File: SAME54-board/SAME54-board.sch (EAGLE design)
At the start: 33 parts, among them IC1 ATSAME54N20A-AUT, J1 GSD09002SEU, J2 CON-SOCJ-2155

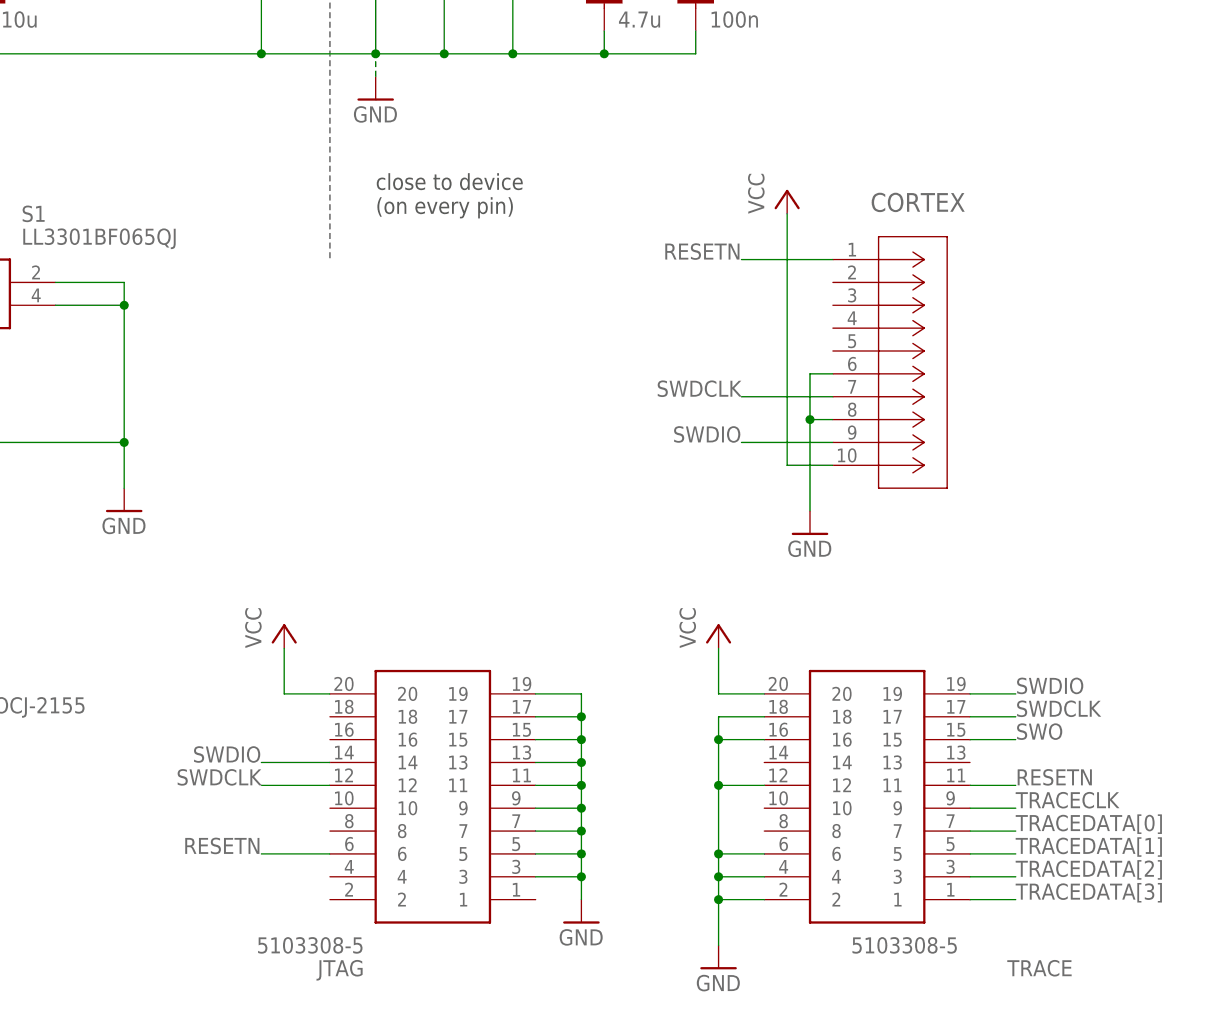
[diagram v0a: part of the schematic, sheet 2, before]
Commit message: Removed molex adapters and recplaed with single pin hole for each signal
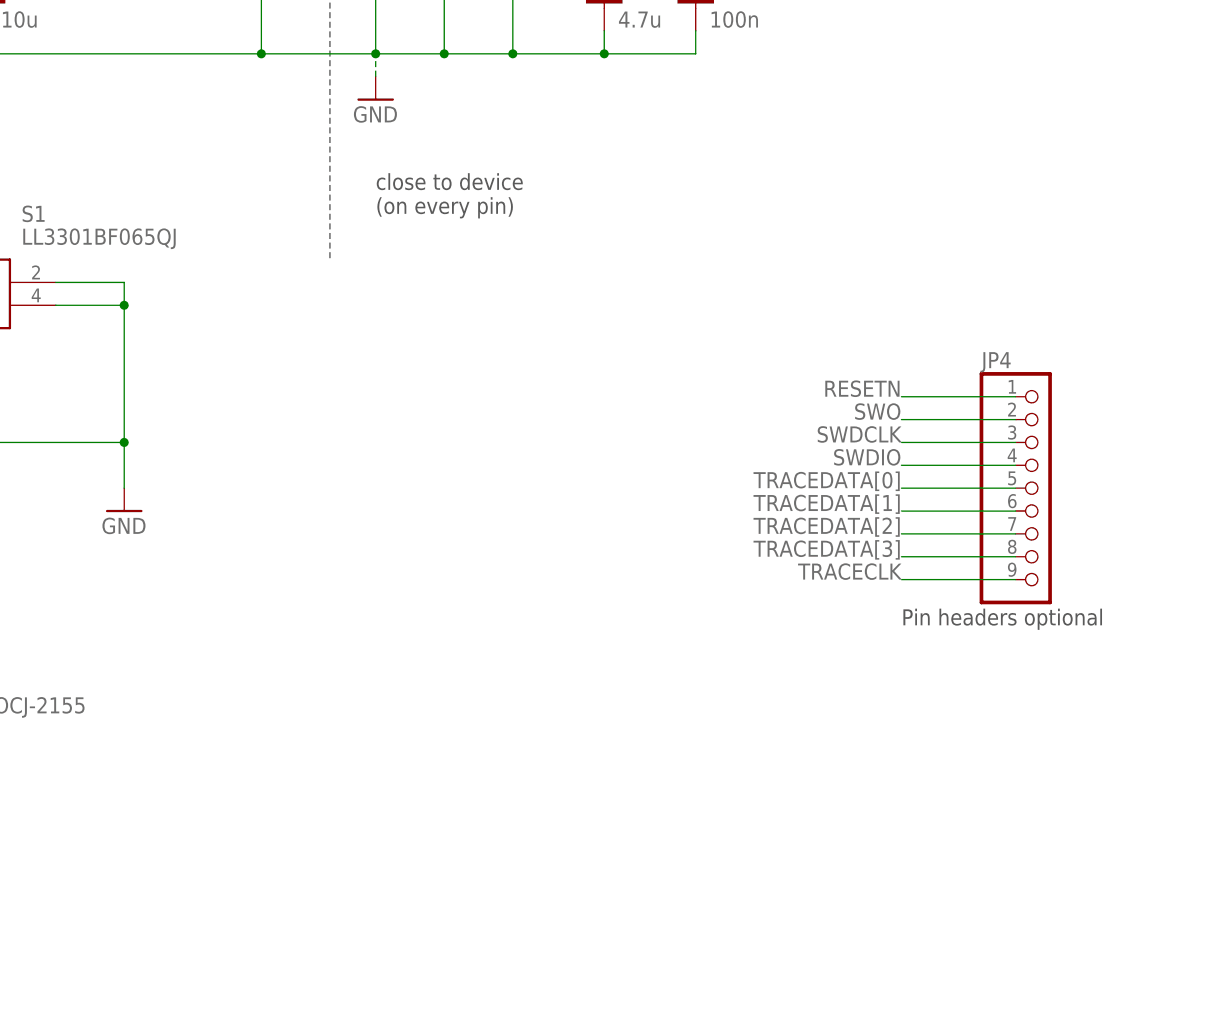
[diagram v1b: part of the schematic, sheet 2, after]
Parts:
- removed CORTEX: 5103308-1, SamacSys_Parts:5103308-1
- removed JTAG, TRACE: 5103308-5, SamacSys_Parts:5103308-5
- added JP4: (no value), pinhead:PINHD-1X9
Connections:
- net GND: no longer CORTEX.6, CORTEX.8, JTAG.11, JTAG.13, JTAG.15, JTAG.17, JTAG.19, JTAG.3, JTAG.5, JTAG.7, JTAG.9, TRACE.12, TRACE.16, TRACE.18, TRACE.2, TRACE.4, TRACE.6
- net RESETN: now also JP4.1; no longer CORTEX.1, JTAG.6, TRACE.11
- net SWDCLK: now also JP4.3; no longer CORTEX.7, JTAG.12, TRACE.17
- net SWDIO: now also JP4.4; no longer CORTEX.9, JTAG.14, TRACE.19
- net SWO: now also JP4.2; no longer TRACE.15
- net TRACECLK: now also JP4.9; no longer TRACE.9
- net TRACEDATA[0]: now also JP4.5; no longer TRACE.7
- net TRACEDATA[1]: now also JP4.6; no longer TRACE.5
- net TRACEDATA[2]: now also JP4.7; no longer TRACE.3
- net TRACEDATA[3]: now also JP4.8; no longer TRACE.1
- net VCC: no longer CORTEX.10, JTAG.20, TRACE.20
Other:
- note added: "Pin headers optional"

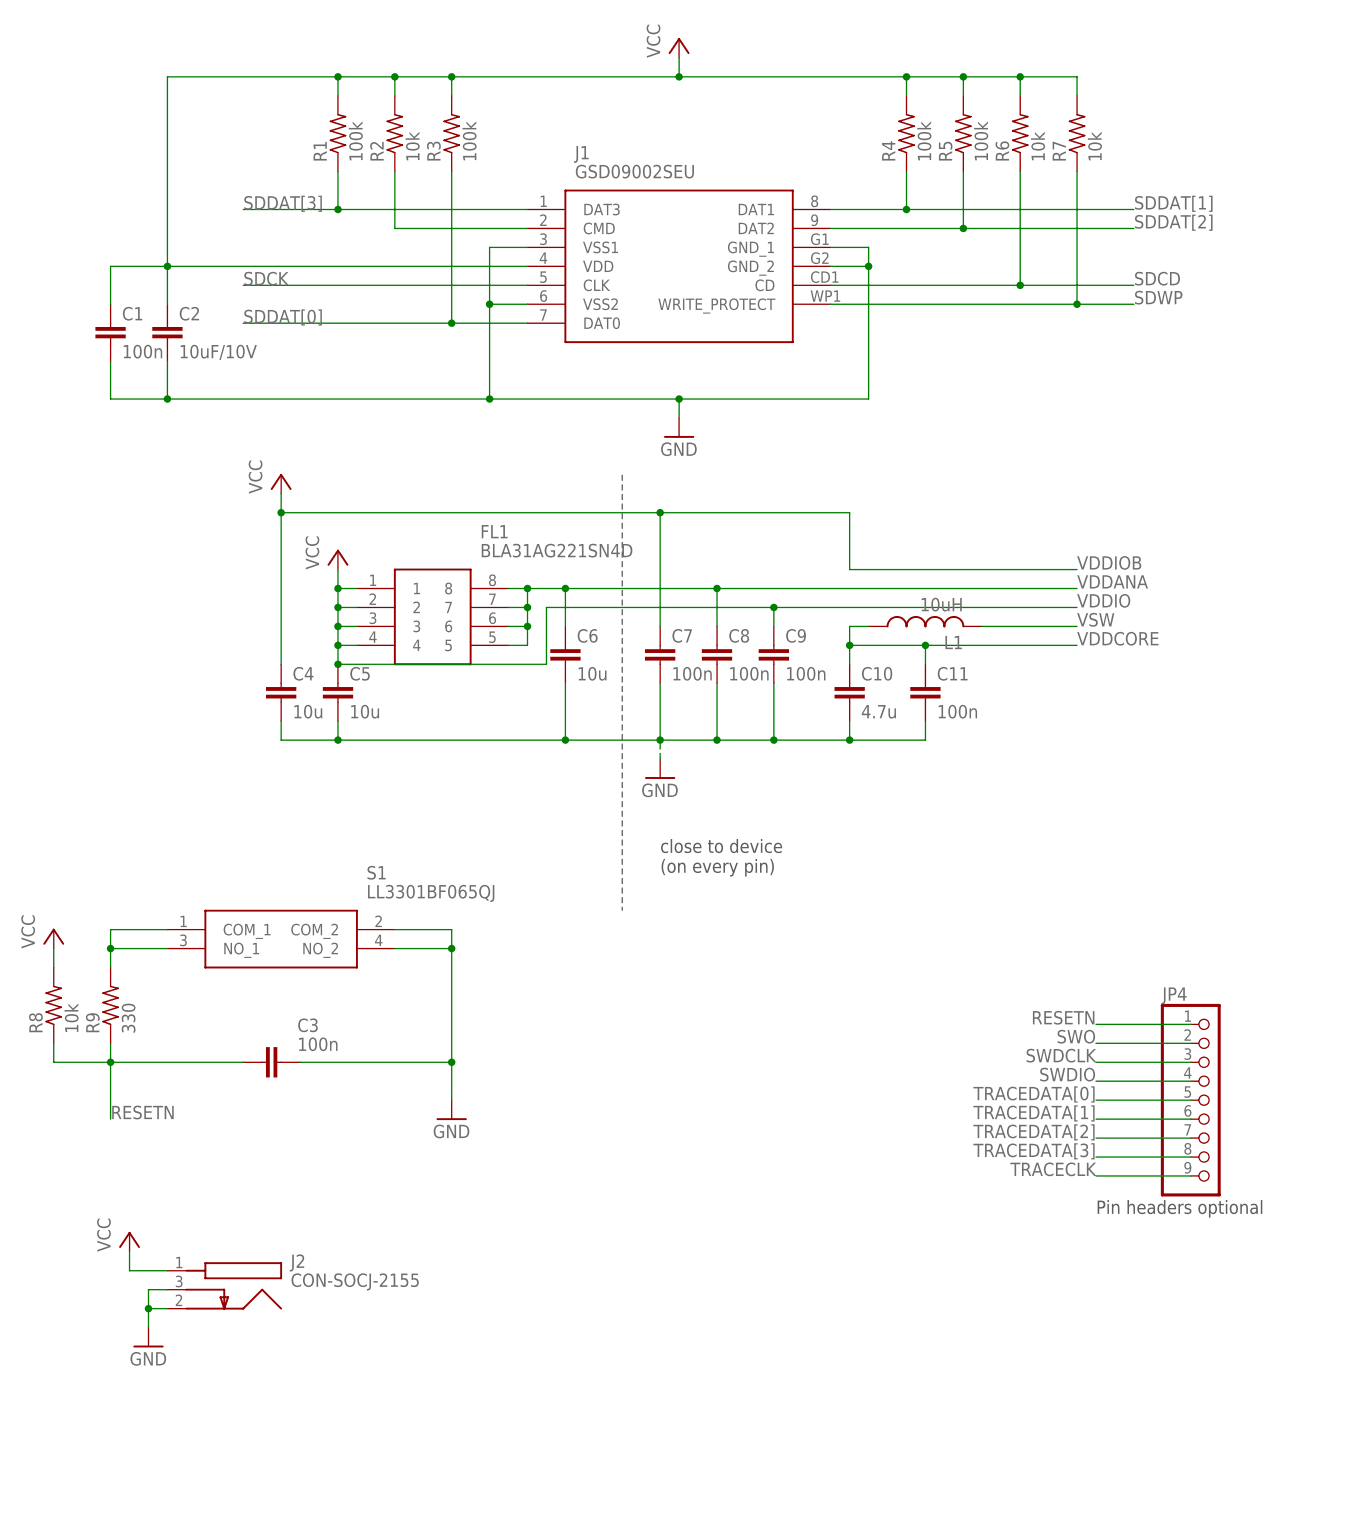
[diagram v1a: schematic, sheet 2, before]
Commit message: Starting new version of board. Bought Microchip development board--will only be printing final product
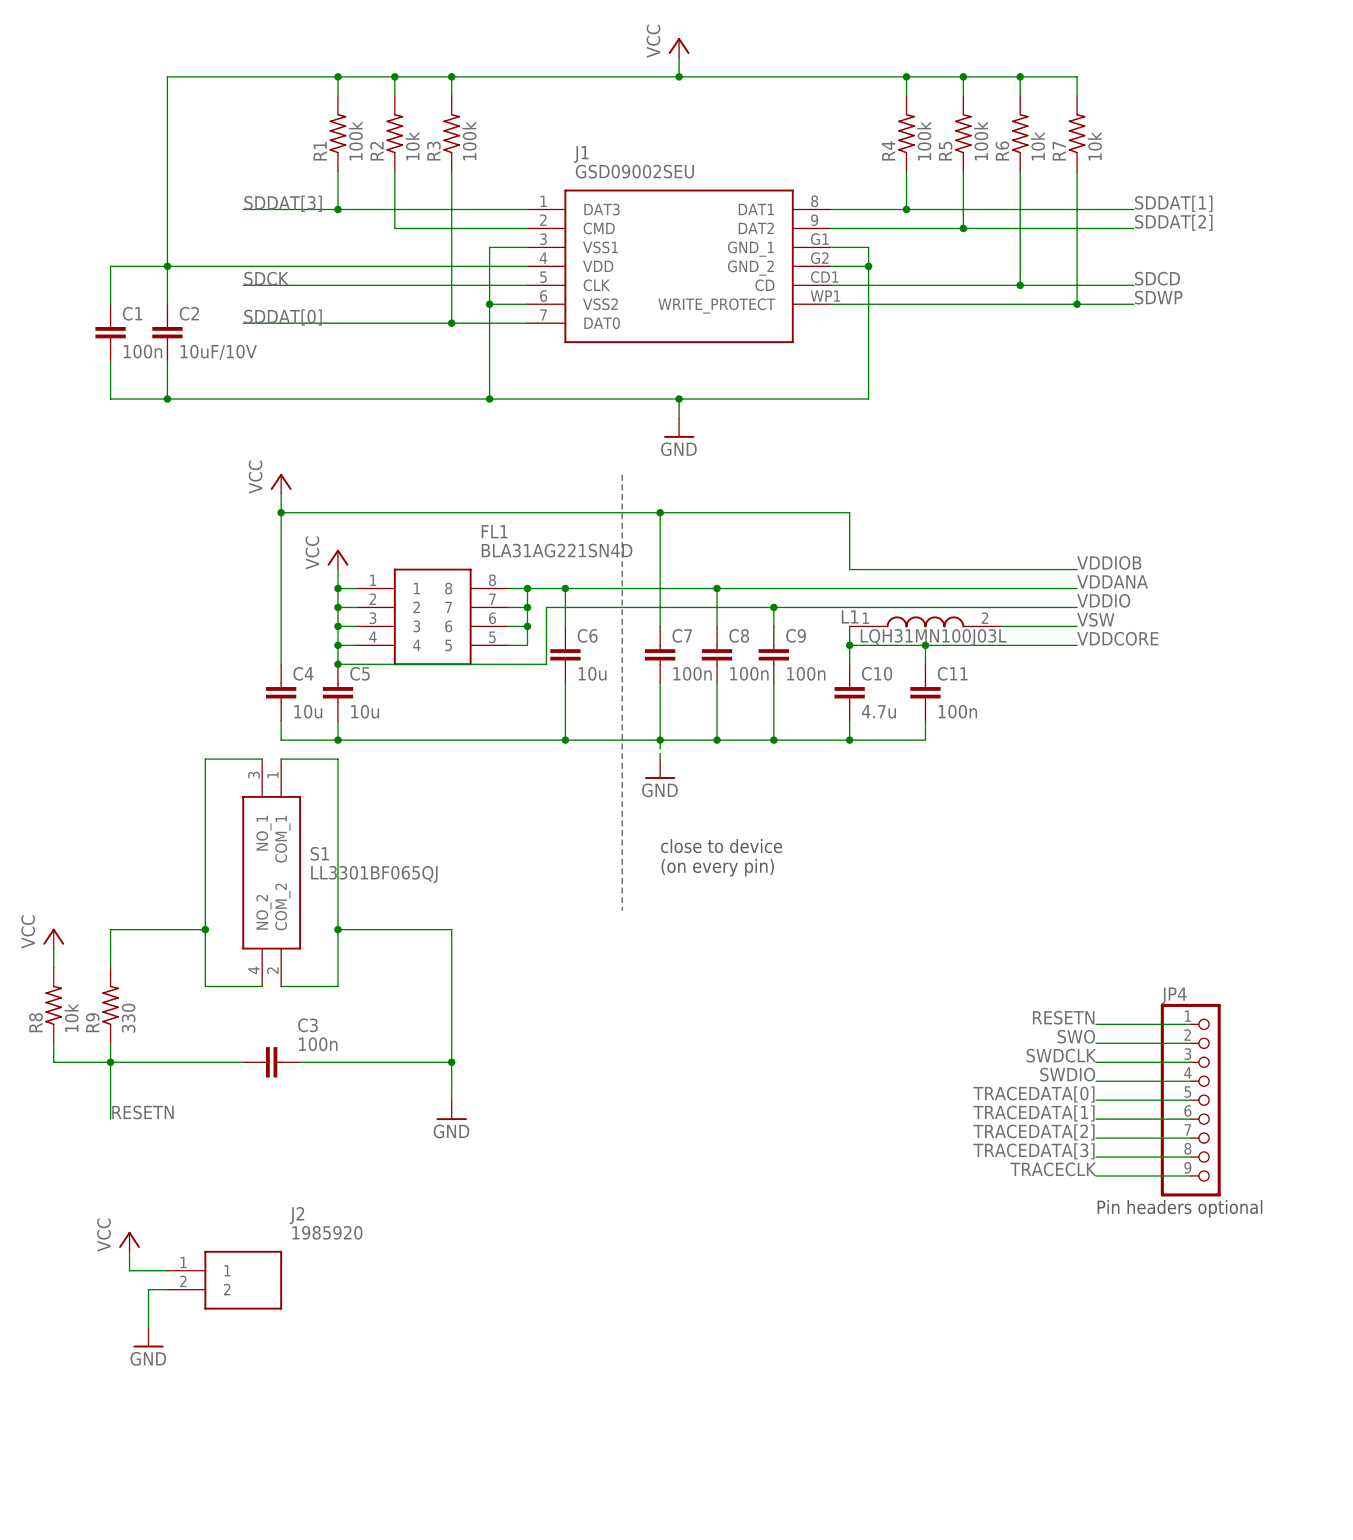
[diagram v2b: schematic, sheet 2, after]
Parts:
- J2: value CON-SOCJ-2155 -> 1985920; device SamacSys_Parts:CON-SOCJ-2155 -> SamacSys_Parts:1985920
- L1: value 10uH -> LQH31MN100J03L; device rcl:L-USL4516C -> SamacSys_Parts:LQH31MN100J03L
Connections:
- net N$24 renamed PA21
- net N$25 renamed PA22
- net N$27 renamed PA24
- net N$28 renamed PA25
- net N$59 renamed PB31
- net N$60 renamed PB0
- net N$61 renamed PB1
- net N$62 renamed PB3
- net N$63 renamed PB2
- net N$64 renamed PB22
- net N$65 renamed PB23
- net N$66 renamed PB24
- net N$67 renamed PB25
- net N$68 renamed PA27
- net GND: now also S1.COM_1; no longer J2.3, S1.NO_2
- net N$4: now also S1.NO_2; no longer S1.COM_1
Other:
- moved on the sheet: S1
